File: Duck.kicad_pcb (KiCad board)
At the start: 2 copper layers, 20 x 110 mm, 34 parts, among them J1 KICK, J2 Aud IN, J3 OUT, J4 EurorackPower, Q1 2N3906, U3 VTL5C, U4 TL084

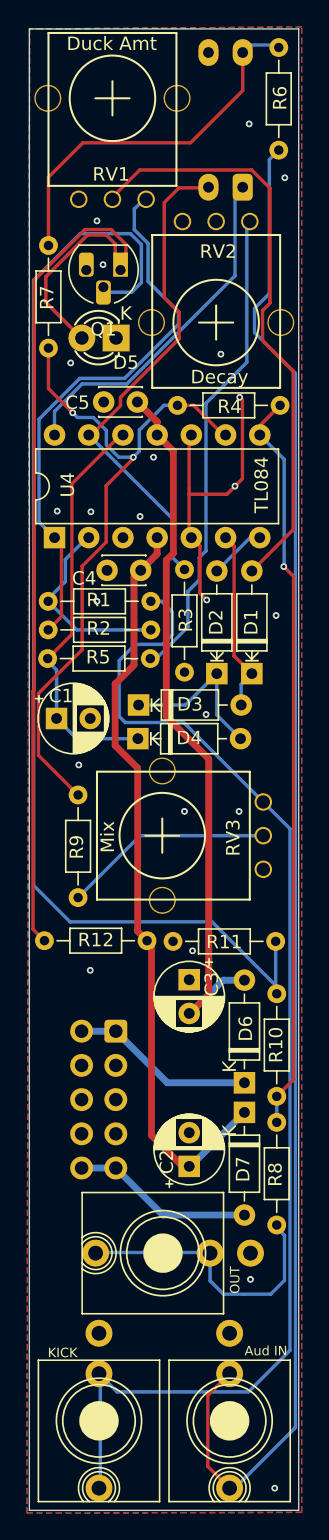
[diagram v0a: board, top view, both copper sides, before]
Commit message: Pot values added to schem and board
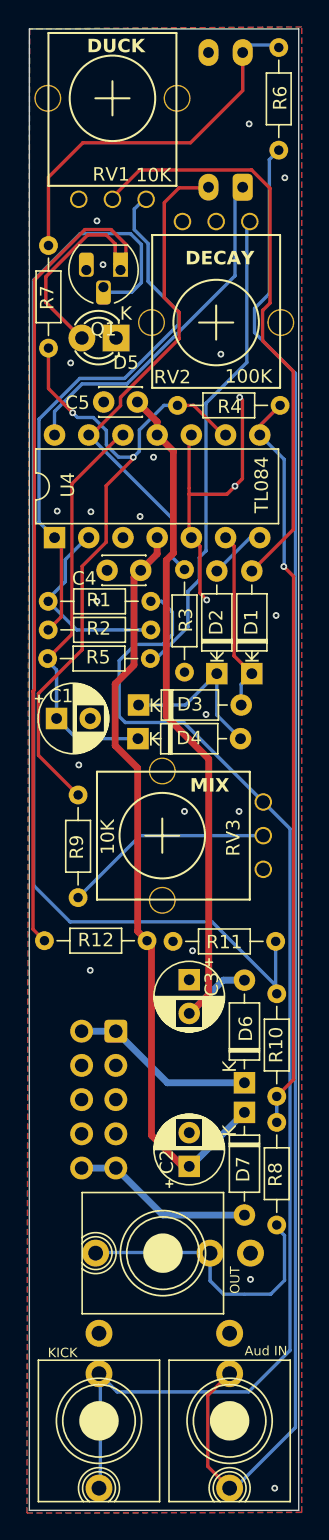
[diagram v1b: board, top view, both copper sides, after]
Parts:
- RV1: value Duck Amt -> 10K
- RV2: value Decay -> 100K
- RV3: value Mix -> 10K
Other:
- board text added: "DECAY"
- board text added: "DUCK"
- board text added: "MIX"
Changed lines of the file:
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@@
   (footprint "Eurocad:Alpha9mmPot" (layer "F.Cu")
     (at 99.95 109.9 90)
+    (property "NOTE" "MIX")
     (property "Sheetfile" "Duck.kicad_sch")
     (property "Sheetname" "")
     (property "ki_description" "Potentiometer")
     (property "ki_keywords" "resistor variable")
-    (property "result" "MIX")
     (attr through_hole)
     (fp_text reference "RV3" (at -0.155 5.27 90) (layer "F.SilkS")
         (effects (font (size 1 1) (thickness 0.15)))
     )
-    (fp_text value "Mix" (at -0.1 -4.05 90) (layer "F.SilkS")
+    (fp_text value "10K" (at -0.1 -4.05 90) (layer "F.SilkS")
         (effects (font (size 1 1) (thickness 0.15)))
     )
@@
   (footprint "Eurocad:Alpha9mmPot" (layer "F.Cu")
     (at 96.25 55.15)
+    (property "NOTE" "Duck Amt")
     (property "Sheetfile" "Duck.kicad_sch")
     (property "Sheetname" "")
@@
         (effects (font (size 1 1) (thickness 0.15)))
     )
-    (fp_text value "Duck Amt" (at -0.05 -4.05) (layer "F.SilkS")
+    (fp_text value "10K" (at 3.05 5.7) (layer "F.SilkS")
         (effects (font (size 1 1) (thickness 0.15)))
     )
@@
   (footprint "Eurocad:Alpha9mmPot" (layer "F.Cu")
     (at 103.95 71.8 180)
+    (property "NOTE" "DECAY")
     (property "Sheetfile" "Duck.kicad_sch")
     (property "Sheetname" "")
     (property "ki_description" "Potentiometer")
     (property "ki_keywords" "resistor variable")
-    (property "result" "DECAY")
     (attr through_hole)
-    (fp_text reference "RV2" (at -0.155 5.27) (layer "F.SilkS")
+    (fp_text reference "RV2" (at 3.25 -4.05) (layer "F.SilkS")
         (effects (font (size 1 1) (thickness 0.15)))
     )
-    (fp_text value "Decay" (at -0.25 -4.05) (layer "F.SilkS")
+    (fp_text value "100K" (at -2.4 -4) (layer "F.SilkS")
         (effects (font (size 1 1) (thickness 0.15)))
     )
@@
     (effects (font (size 0.8 0.8) (thickness 0.15) bold italic) (justify left bottom mirror))
   )
+  (gr_text "DECAY" (at 101.65 67.6) (layer "F.SilkS")
+    (effects (font (size 1 1) (thickness 0.2) bold) (justify left bottom))
+  )
+  (gr_text "MIX" (at 102 106.75) (layer "F.SilkS")
+    (effects (font (size 1 1) (thickness 0.2) bold) (justify left bottom))
+  )
+  (gr_text "DUCK" (at 94.35 51.85) (layer "F.SilkS")
+    (effects (font (size 1 1) (thickness 0.2) bold) (justify left bottom))
+  )
   (segment (start 105.279999 88.399999) (end 105.279999 96.549999) (width 0.254) (layer "F.Cu") (net 1))
